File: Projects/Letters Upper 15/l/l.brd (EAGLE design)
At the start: 16.5 x 21.6 mm, 27 parts

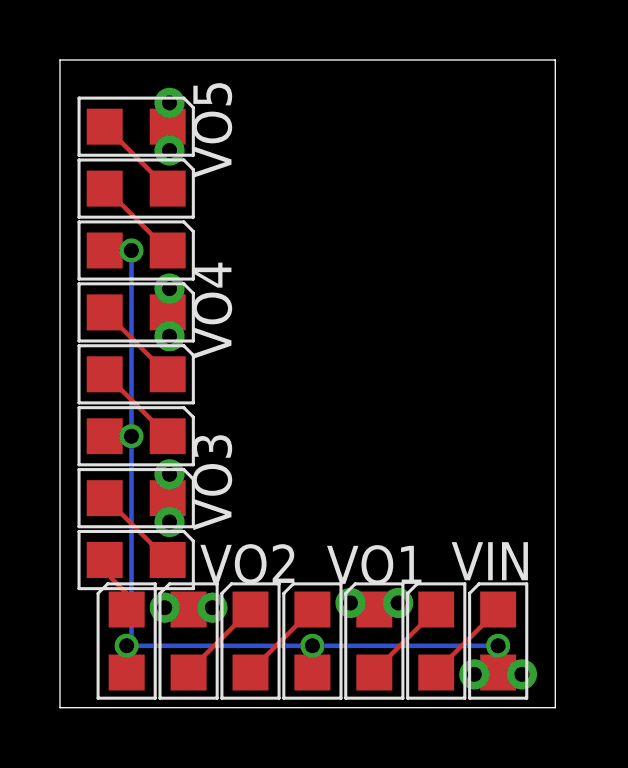
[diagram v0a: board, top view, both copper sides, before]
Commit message: 
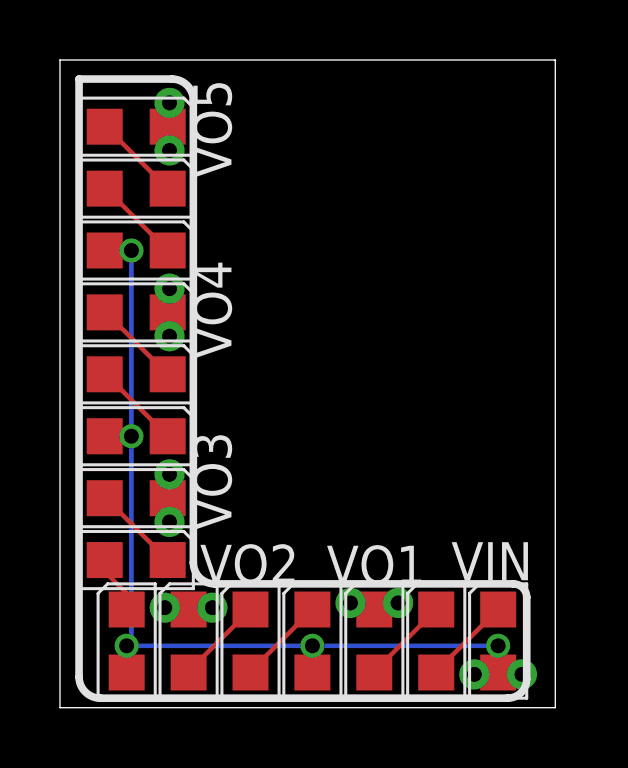
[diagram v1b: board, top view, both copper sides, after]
